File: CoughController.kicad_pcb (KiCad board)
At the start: 2 copper layers, 125 x 100 mm, 61 parts, among them J1 SW1, J10 AUDIO_IN, J11 AUDIO_OUT, J12 DI-2, J13 DO-2, J14 CD1/CD2, J15 CF/MD, J16 IN1/IN2, J17 IN3/IN4, J18 Out, J19 In, J2 SW2, J3 SW3, J4 SW4, J5 SW5, J6 PWR_IN, J7 PWR_OUT, J8 DI-1, J9 DO-1, K1 G6A-274P-ST-US DC12, K2 G6A-274P-ST-US DC12, U1 TLP627-2, U2 TLP627-2, U3 TLP627-2, U4 TLP627-2, U5 TLP627-2, U6 TLP627-2, U7 TLP627-2, U8 TLP627-2

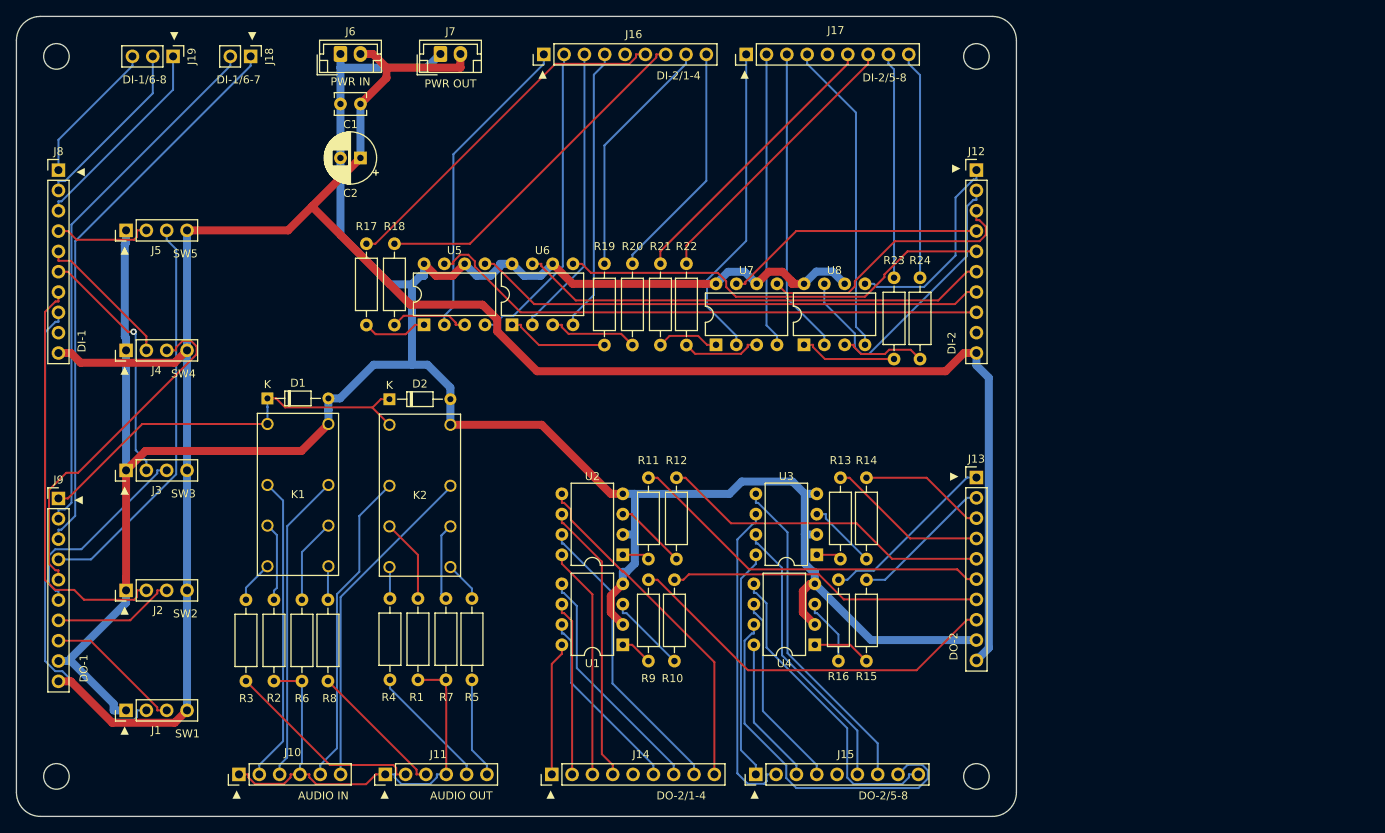
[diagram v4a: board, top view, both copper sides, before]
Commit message: 端子をピンヘッダ2x10に変更
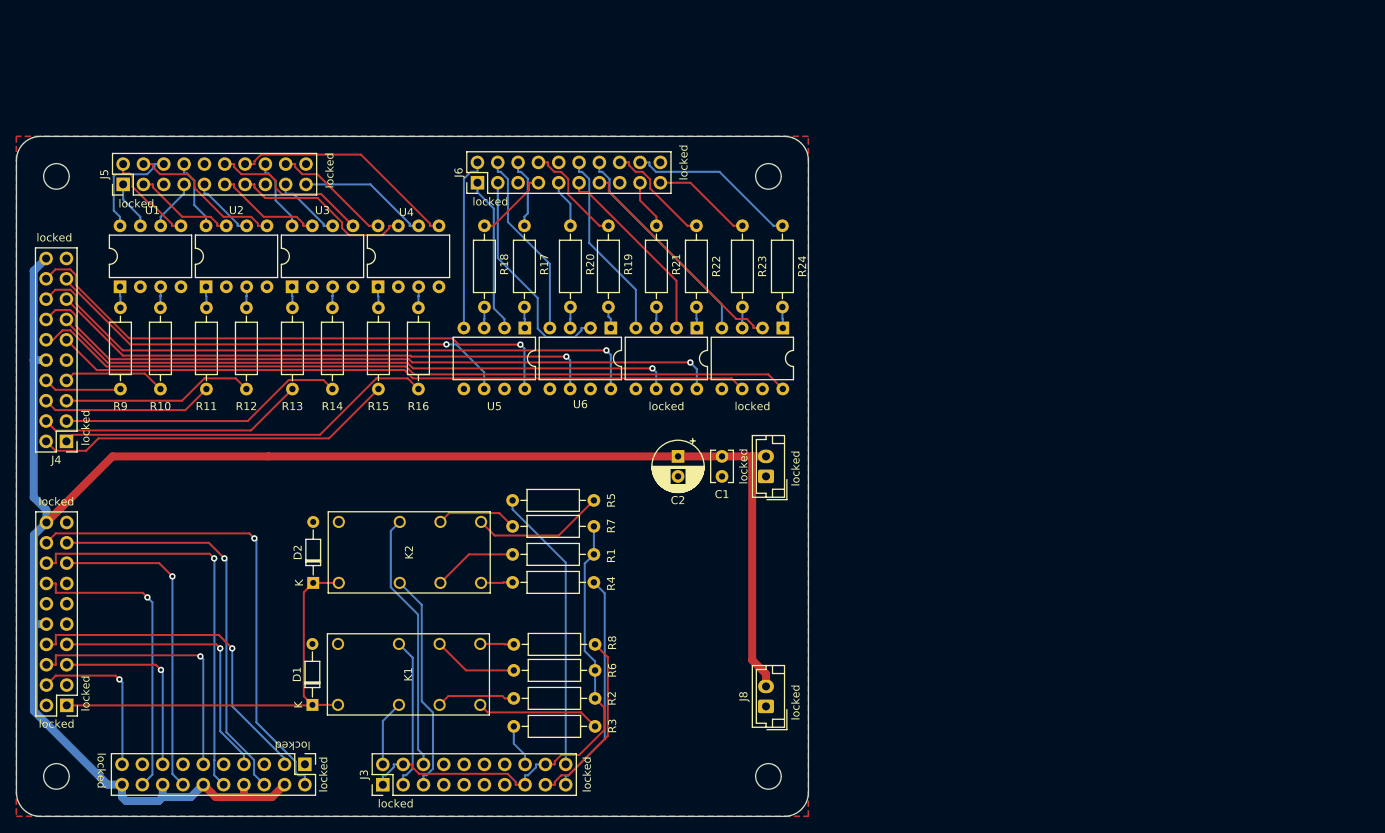
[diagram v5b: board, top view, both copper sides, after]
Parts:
- removed J1: SW1, Connector_PinHeader_2.54mm:PinHeader_1x04_P2.54mm_Vertical
- removed J10: AUDIO_IN, Connector_PinHeader_2.54mm:PinHeader_1x06_P2.54mm_Vertical
- removed J11: AUDIO_OUT, Connector_PinHeader_2.54mm:PinHeader_1x06_P2.54mm_Vertical
- removed J12: DI-2, Connector_PinHeader_2.54mm:PinHeader_1x10_P2.54mm_Vertical
- removed J13: DO-2, Connector_PinHeader_2.54mm:PinHeader_1x10_P2.54mm_Vertical
- removed J14: CD1/CD2, Connector_PinHeader_2.54mm:PinHeader_1x09_P2.54mm_Vertical
- removed J15: CF/MD, Connector_PinHeader_2.54mm:PinHeader_1x09_P2.54mm_Vertical
- removed J16: IN1/IN2, Connector_PinHeader_2.54mm:PinHeader_1x09_P2.54mm_Vertical
- removed J17: IN3/IN4, Connector_PinHeader_2.54mm:PinHeader_1x09_P2.54mm_Vertical
- removed J18: Out, Connector_PinHeader_2.54mm:PinHeader_1x02_P2.54mm_Vertical
- removed J19: In, Connector_PinHeader_2.54mm:PinHeader_1x03_P2.54mm_Vertical
- removed J2: SW2, Connector_PinHeader_2.54mm:PinHeader_1x04_P2.54mm_Vertical
- removed J9: DO-1, Connector_PinHeader_2.54mm:PinHeader_1x10_P2.54mm_Vertical
- added J6: GPIO-IN, Connector_PinHeader_2.54mm:PinHeader_2x10_P2.54mm_Vertical, F.Cu at (107.6, 70.8)
- added locked: SW1-5, Connector_PinHeader_2.54mm:PinHeader_2x10_P2.54mm_Vertical, F.Cu at (86.1, 143.5)
- J3: value SW3 -> AUDIO IN/OUT; footprint Connector_PinHeader_2.54mm:PinHeader_1x04_P2.54mm_Vertical -> Connector_PinHeader_2.54mm:PinHeader_2x10_P2.54mm_Vertical
- J4: value SW4 -> DIO-2; footprint Connector_PinHeader_2.54mm:PinHeader_1x04_P2.54mm_Vertical -> Connector_PinHeader_2.54mm:PinHeader_2x10_P2.54mm_Vertical
- J5: value SW5 -> GPIO-OUT; footprint Connector_PinHeader_2.54mm:PinHeader_1x04_P2.54mm_Vertical -> Connector_PinHeader_2.54mm:PinHeader_2x10_P2.54mm_Vertical
- locked: renamed from J8; value DI-1 -> DIO-1; footprint Connector_PinHeader_2.54mm:PinHeader_1x10_P2.54mm_Vertical -> Connector_PinHeader_2.54mm:PinHeader_2x10_P2.54mm_Vertical
- moved J8 91.1 mm to (143.7, 136.2), turned to 90 degrees
- moved R9 79.4 mm to (63.0, 86.4), turned to -90 degrees
- moved R10 78.0 mm to (68.0, 86.4), turned to -90 degrees
- moved U1 77.2 mm to (63.0, 83.8), turned to 90 degrees
- moved R13 75.4 mm to (84.5, 86.4), turned to -90 degrees
- moved R15 75.3 mm to (95.2, 86.4), turned to -90 degrees
- moved locked 75.0 mm to (143.7, 107.5), turned to 90 degrees
- moved R14 73.8 mm to (89.5, 86.4), turned to -90 degrees
- moved U3 73.7 mm to (84.5, 83.8), turned to 90 degrees
- moved U4 70.6 mm to (95.2, 83.8), turned to 90 degrees
- moved R16 68.6 mm to (100.2, 86.4), turned to -90 degrees
- moved locked 66.9 mm to (56.3, 136.1), turned to 180 degrees
- moved R11 63.6 mm to (73.8, 86.4), turned to -90 degrees
- moved C1 63.1 mm to (138.2, 105.0), turned to -90 degrees
- moved R12 62.3 mm to (78.8, 86.4), turned to -90 degrees
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- renumbered J7 to J8, U8 to locked, U7 to locked, J6 to locked
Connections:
- J3 pad 1: MCOM1 -> AUDIO-IN-L-GND
- J3 pad 2: Net-(J3-Pin_2) -> AUDIO-IN-L-HOT
- J3 pad 3: Net-(J3-Pin_3) -> AUDIO-IN-L-COLD
- J3 pad 4: COM0 -> AUDIO-IN-L-GND
- J4 pad 1: MCOM1 -> DIO-2/OUT8
- J4 pad 2: Net-(J4-Pin_2) -> DIO-2/OUT7
- J4 pad 3: Net-(J4-Pin_3) -> DIO-2/OUT6
- J4 pad 4: COM0 -> DIO-2/OUT5
- J5 pad 1: MCOM1 -> GPIO-OUT/1M
- J5 pad 2: Net-(J5-Pin_2) -> GPIO-OUT/2M
- J5 pad 3: Net-(J5-Pin_3) -> GPIO-OUT/3M
- J5 pad 4: COM0 -> GPIO-OUT/4M
- K1 pad 13: Net-(J10-Pin_3) -> AUDIO-IN-L-COLD
- K1 pad 4: Net-(J10-Pin_2) -> AUDIO-IN-L-HOT
- K2 pad 13: Net-(J10-Pin_6) -> AUDIO-IN-R-COLD
- K2 pad 4: Net-(J10-Pin_5) -> AUDIO-IN-R-HOT
- R1 pad 1: Net-(J10-Pin_1) -> AUDIO-IN-L-GND
- R10 pad 2: Net-(J13-Pin_7) -> DIO-2/OUT2
- R11 pad 2: Net-(J13-Pin_6) -> DIO-2/OUT3
- R12 pad 2: Net-(J13-Pin_5) -> DIO-2/OUT4
- R13 pad 2: Net-(J13-Pin_4) -> DIO-2/OUT5
- R14 pad 2: Net-(J13-Pin_3) -> DIO-2/OUT6
- R15 pad 2: Net-(J13-Pin_2) -> DIO-2/OUT7
- R16 pad 2: Net-(J13-Pin_1) -> DIO-2/OUT8
- R17 pad 2: Net-(J16-Pin_6) -> GPIO-IN/1P
- R18 pad 2: Net-(J16-Pin_7) -> GPIO-IN/2P
- R19 pad 2: Net-(J16-Pin_8) -> GPIO-IN/3P
- R2 pad 1: Net-(J10-Pin_1) -> AUDIO-IN-L-GND
- R20 pad 2: Net-(J16-Pin_9) -> GPIO-IN/4P
- R21 pad 2: Net-(J17-Pin_6) -> GPIO-IN/6P
- R22 pad 2: Net-(J17-Pin_7) -> GPIO-IN/5P
- R23 pad 2: Net-(J17-Pin_8) -> GPIO-IN/8P
- R24 pad 2: Net-(J17-Pin_9) -> GPIO-IN/7P
- R3 pad 1: Net-(J11-Pin_2) -> Net-(K1-Pad8)
- R3 pad 2: Net-(K1-Pad8) -> AUDIO-OUT-L-HOT
- R4 pad 1: Net-(J11-Pin_5) -> AUDIO-OUT-R-HOT
- R5 pad 1: Net-(J11-Pin_6) -> Net-(K2-Pad9)
- R5 pad 2: Net-(K2-Pad9) -> AUDIO-OUT-R-COLD
- R6 pad 2: Net-(J10-Pin_1) -> AUDIO-IN-L-GND
- R7 pad 2: Net-(J10-Pin_1) -> AUDIO-IN-L-GND
- R8 pad 1: Net-(J11-Pin_3) -> AUDIO-OUT-L-COLD
- R9 pad 2: Net-(J13-Pin_8) -> DIO-2/OUT1
- U1 pad 5: Net-(J14-Pin_7) -> GPIO-OUT/2M
- U1 pad 6: Net-(J14-Pin_2) -> GPIO-OUT/2P
- U1 pad 7: Net-(J14-Pin_6) -> GPIO-OUT/1M
- U1 pad 8: Net-(J14-Pin_1) -> GPIO-OUT/1P
- U2 pad 5: Net-(J14-Pin_9) -> GPIO-OUT/4M
- U2 pad 6: Net-(J14-Pin_4) -> GPIO-OUT/4P
- U2 pad 7: Net-(J14-Pin_8) -> GPIO-OUT/3M
- U2 pad 8: Net-(J14-Pin_3) -> GPIO-OUT/3P
- U3 pad 5: Net-(J15-Pin_7) -> GPIO-OUT/6M
- U3 pad 6: Net-(J15-Pin_2) -> GPIO-OUT/6P
- U3 pad 7: Net-(J15-Pin_6) -> GPIO-OUT/5M
- U3 pad 8: Net-(J15-Pin_1) -> GPIO-OUT/5P
- U4 pad 5: Net-(J15-Pin_9) -> GPIO-OUT/8M
- U4 pad 6: Net-(J15-Pin_4) -> GPIO-OUT/8P
- U4 pad 7: Net-(J15-Pin_8) -> GPIO-OUT/7M
- U4 pad 8: Net-(J15-Pin_3) -> GPIO-OUT/7P
- U5 pad 2: Net-(J16-Pin_1) -> GPIO-IN/1M
- U5 pad 4: Net-(J16-Pin_2) -> GPIO-IN/2M
- U5 pad 5: Net-(J12-Pin_7) -> MCOM1
- U5 pad 6: MCOM1 -> DIO-2/IN2
- U5 pad 7: Net-(J12-Pin_8) -> MCOM1
- U5 pad 8: MCOM1 -> DIO-2/IN1
- U6 pad 2: Net-(J16-Pin_3) -> GPIO-IN/3M
- U6 pad 4: Net-(J16-Pin_4) -> GPIO-IN/4M
- U6 pad 5: Net-(J12-Pin_5) -> MCOM1
- U6 pad 6: MCOM1 -> DIO-2/IN4
- U6 pad 7: Net-(J12-Pin_6) -> MCOM1
- U6 pad 8: MCOM1 -> DIO-2/IN3
- locked pad 1: Net-(R23-Pad1) -> Net-(R24-Pad1)
- locked pad 2: Net-(J17-Pin_3) -> GPIO-IN/7M
- locked pad 3: Net-(R24-Pad1) -> Net-(R23-Pad1)
- locked pad 4: Net-(J17-Pin_4) -> GPIO-IN/8M
- locked pad 5: Net-(J12-Pin_1) -> MCOM1
- locked pad 6: MCOM1 -> DIO-2/IN8
- locked pad 7: Net-(J12-Pin_2) -> MCOM1
- locked pad 8: MCOM1 -> DIO-2/IN7
- locked pad 1: Net-(J19-Pin_3) -> RY_POW
- locked pad 2: Net-(J19-Pin_2) -> unconnected-(J2-Pin_2-Pad2)
- locked pad 3: Net-(J19-Pin_1) -> unconnected-(J2-Pin_3-Pad3)
- locked pad 4: Net-(J5-Pin_2) -> SW5/L1
- locked pad 5: Net-(J4-Pin_2) -> SW4/L1
- locked pad 6: Net-(J3-Pin_2) -> SW3/L1
- locked pad 7: Net-(J2-Pin_2) -> SW2/L1
- locked pad 8: Net-(J1-Pin_2) -> SW1/L1
- locked pad 9: unconnected-(J8-Pin_9-Pad9) -> MCOM1
- locked pad 1: Net-(R21-Pad1) -> Net-(R22-Pad1)
- locked pad 2: Net-(J17-Pin_1) -> GPIO-IN/5M
- locked pad 3: Net-(R22-Pad1) -> Net-(R21-Pad1)
- locked pad 4: Net-(J17-Pin_2) -> GPIO-IN/6M
- locked pad 5: Net-(J12-Pin_3) -> MCOM1
- locked pad 6: MCOM1 -> DIO-2/IN6
- locked pad 7: Net-(J12-Pin_4) -> MCOM1
- locked pad 8: MCOM1 -> DIO-2/IN5
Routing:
- net MCOM1: track 358.2 -> 0.00 mm
- net DIO-2/IN7: track 0.00 -> 95.6 mm
- net DIO-2/IN5: track 0.00 -> 88.1 mm, vias 0 -> 1
- net DIO-2/IN8: track 0.00 -> 87.0 mm
- net DIO-2/IN3: track 0.00 -> 79.3 mm, vias 0 -> 1
- net DIO-2/IN6: track 0.00 -> 78.7 mm, vias 0 -> 1
- net Net-(J12-Pin_8): track 70.5 -> 0.00 mm
- net Net-(J18-Pin_1): track 70.5 -> 0.00 mm
- net DIO-2/IN1: track 0.00 -> 70.2 mm, vias 0 -> 1
- net DIO-2/IN4: track 0.00 -> 69.7 mm, vias 0 -> 1
- net Net-(J18-Pin_2): track 67.2 -> 0.00 mm
- net Net-(J12-Pin_7): track 64.1 -> 0.00 mm
- net AUDIO-IN-L-GND: track 0.00 -> 62.0 mm
- net Net-(J1-Pin_2): track 61.2 -> 0.00 mm
- net SW1/O: track 0.00 -> 60.6 mm, vias 0 -> 1
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- added copper zone on B.Cu, net MCOM1
- added copper zone on F.Cu, net MCOM1
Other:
- board size 125 x 100 mm -> 99 x 85 mm
- board text added: "locked"
- board text removed: "AUDIO IN"
- board text removed: "AUDIO OUT"
- board text removed: "DI-1"
- board text removed: "DI-1/6-7"
- board text removed: "DI-1/6-8"
- board text removed: "DI-2"
- board text removed: "DI-2/1-4"
- board text removed: "DI-2/5-8"
- board text removed: "DO-1"
- board text removed: "DO-2"
- board text removed: "DO-2/1-4"
- board text removed: "DO-2/5-8"
- board text removed: "PWR IN"
- board text removed: "PWR OUT"
- board text removed: "SW1"
- board text removed: "SW2"
- board text removed: "SW3"
- board text removed: "SW4"
- board text removed: "SW5"
- board text removed: "▲"

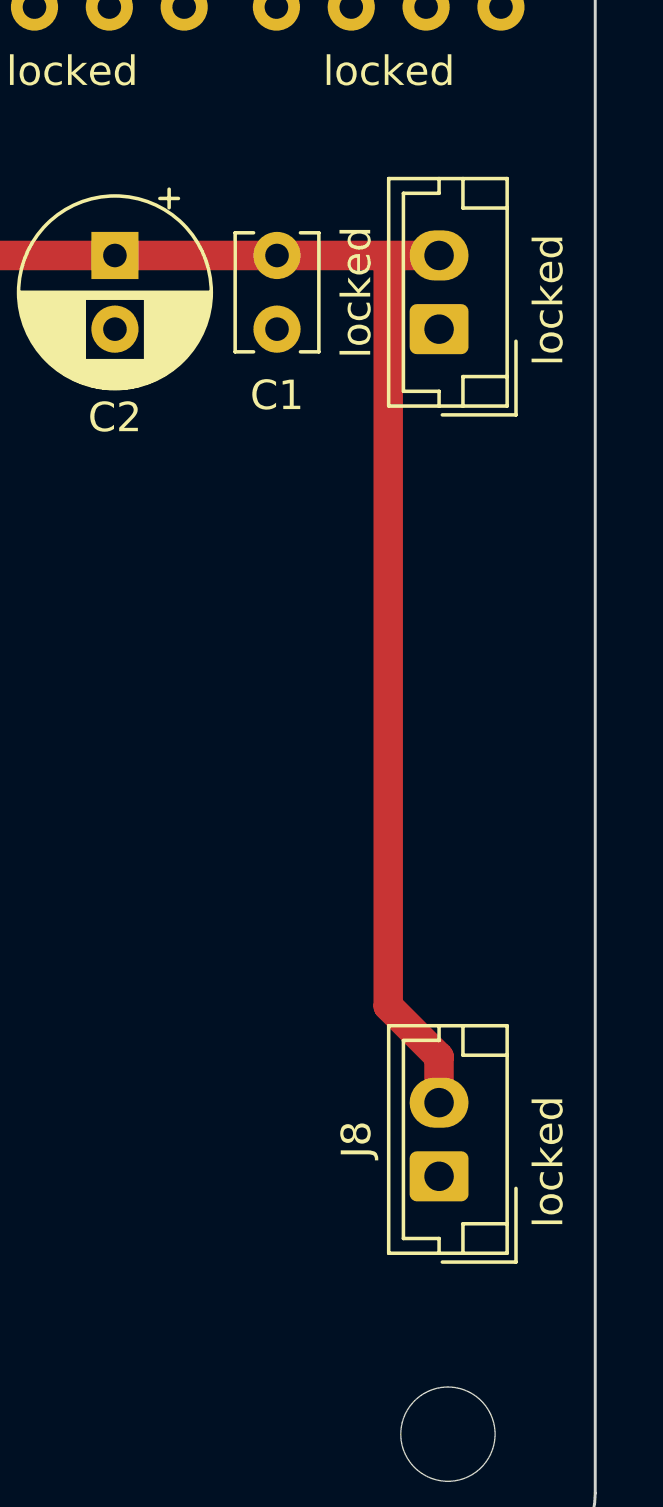
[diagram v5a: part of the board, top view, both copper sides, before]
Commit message: 電源コネクタ　フットプリント間違いを修正
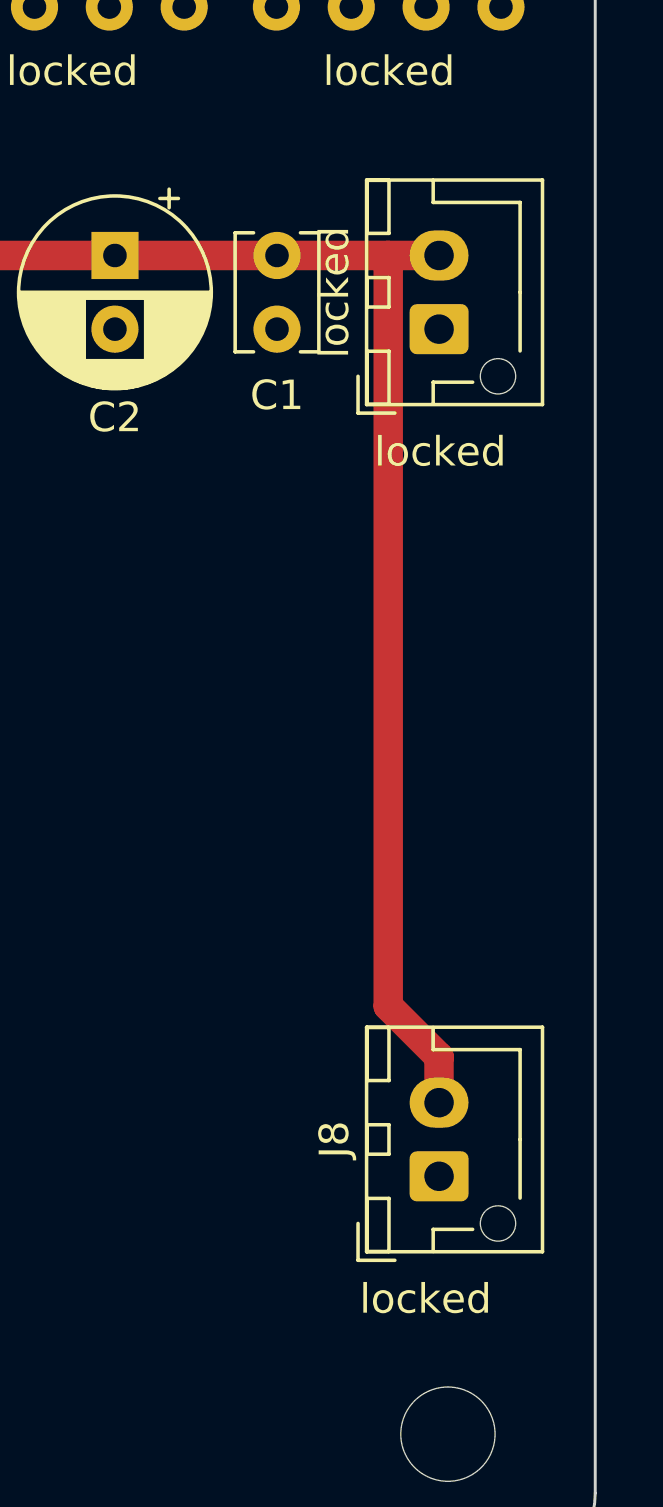
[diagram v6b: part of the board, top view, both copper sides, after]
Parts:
- J8, locked: footprint Connector_JST:JST_EH_B2B-EH-A_1x02_P2.50mm_Vertical -> Connector_JST:JST_XH_B2B-XH-AM_1x02_P2.50mm_Vertical

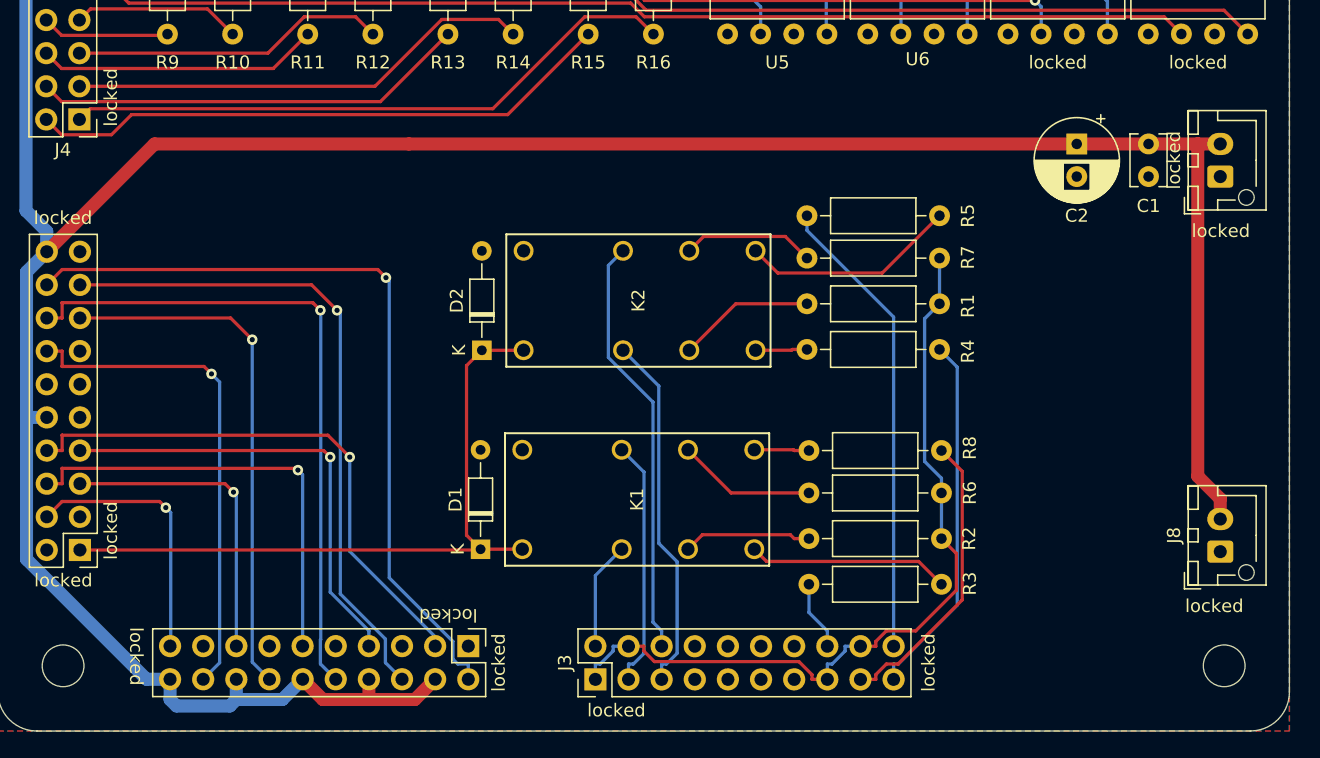
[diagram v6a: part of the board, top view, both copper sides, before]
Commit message: リレーのフットプリントが間違っていたのを修正
ピン配置が間違っていた
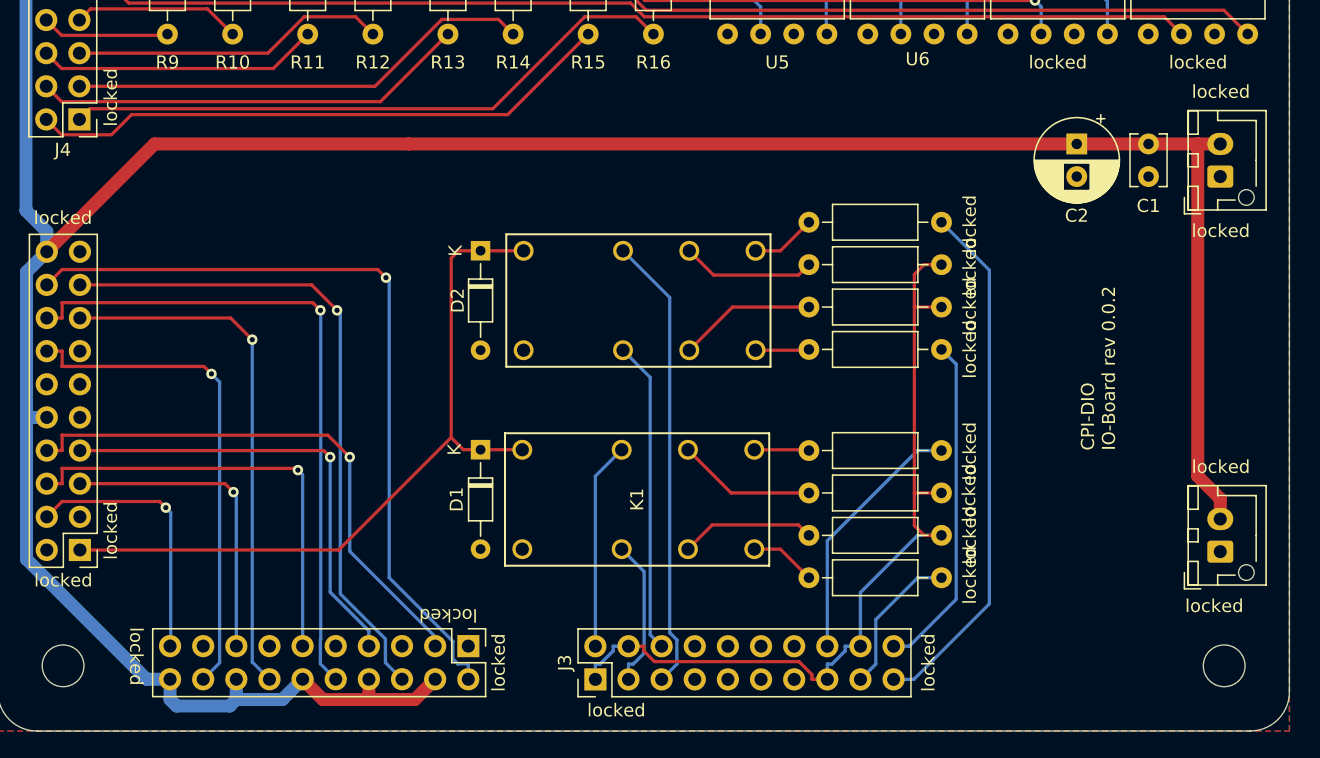
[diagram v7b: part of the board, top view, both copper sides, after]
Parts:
- moved locked 14.4 mm to (112.2, 128.5), turned to 0 degrees
- moved locked 14.3 mm to (112.2, 120.8), turned to 0 degrees
- moved locked 9.75 mm to (122.3, 111.0)
- moved locked 9.75 mm to (122.3, 138.2)
- moved D2 7.63 mm to (87.0, 113.2), turned to -90 degrees
- moved D1 7.63 mm to (87.0, 128.4), turned to -90 degrees
- moved locked 3.75 mm to (112.2, 117.5)
- moved locked 3.50 mm to (122.3, 131.8)
- moved locked 3.25 mm to (112.2, 135.0)
- moved locked 3.00 mm to (122.3, 114.2)
- renumbered R1 to locked, J8 to locked, R4 to locked, R3 to locked, R8 to locked, R6 to locked, R7 to locked, R5 to locked, R2 to locked
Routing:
- net AUDIO-OUT-L-HOT: track 5.33 -> 19.7 mm
- net Net-(K2-Pad9): track 16.6 -> 4.11 mm
- net AUDIO-OUT-R-HOT: track 28.1 -> 40.5 mm
- net Net-(K1-Pad8): track 15.5 -> 4.21 mm
- net AUDIO-OUT-L-COLD: track 22.6 -> 11.4 mm
- net AUDIO-OUT-R-COLD: track 35.8 -> 25.9 mm
- net AUDIO-IN-R-COLD: track 32.5 -> 23.9 mm
- net AUDIO-IN-L-HOT: track 8.28 -> 15.9 mm
- net AUDIO-IN-L-COLD: track 19.0 -> 11.4 mm
- net AUDIO-IN-R-HOT: track 27.7 -> 35.0 mm
- net RY_POW: track 53.3 -> 57.4 mm
- net AUDIO-IN-L-GND: track 62.0 -> 66.0 mm
- net Net-(K2-Pad8): track 3.96 -> 5.00 mm
- net Net-(K1-Pad9): track 4.21 -> 5.10 mm
- net Net-(K1-Pad6): track 9.85 -> 10.6 mm
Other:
- board text added: "CPI-DIO IO-Board rev 0.0.2"
